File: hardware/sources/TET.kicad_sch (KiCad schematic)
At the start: 43 parts, among them J1 SWD, M1 MountingHole, M2 MountingHole, M3 MountingHole, M4 MountingHole, U1 TCAN330GDCNR, U2 8 MHz, U3 STM32L431RBT6TR, U4 TMP112AIDRLR

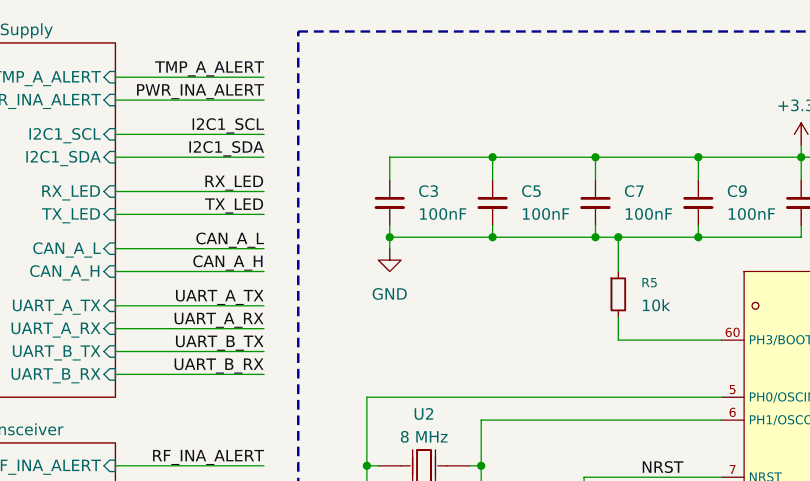
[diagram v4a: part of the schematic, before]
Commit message: hardware(schematic): add bulk capacitor on STM32L4 #5
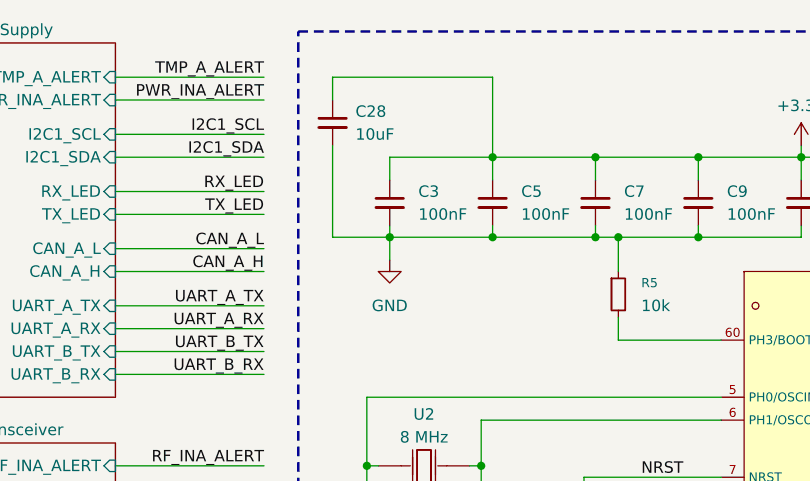
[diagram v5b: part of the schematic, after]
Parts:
- added C28: 10uF, symbol Device:C_Small
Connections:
- net +3.3V: now also C28.1
- net GND: now also C28.2

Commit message: feat(schematic): fix double pull-up resistor for LR_BUSY
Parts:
- removed R2: 10k, Resistor_SMD:R_0603_1608Metric, symbol Device:R_Small
- C28: footprint (none) -> Capacitor_SMD:C_0603_1608Metric
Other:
- moved on the sheet: R1
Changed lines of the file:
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@@
 	)
 	(junction
-		(at 62.23 101.6)
-		(diameter 0)
-		(color 0 0 0 0)
-	)
-	(junction
 		(at 154.94 27.94)
 		(diameter 0)
@@
 	(wire
 		(pts
-			(xy 69.85 101.6) (xy 69.85 102.87)
-		)
-		(stroke
-			(width 0)
-			(type default)
-		)
-	)
-	(wire
-		(pts
 			(xy 201.93 30.48) (xy 209.55 30.48)
 		)
@@
 	(wire
 		(pts
-			(xy 62.23 99.06) (xy 62.23 101.6)
+			(xy 71.12 102.87) (xy 71.12 107.95)
 		)
 		(stroke
@@
 	(wire
 		(pts
-			(xy 62.23 115.57) (xy 62.23 111.76)
+			(xy 71.12 115.57) (xy 71.12 113.03)
 		)
 		(stroke
@@
 	(wire
 		(pts
-			(xy 62.23 106.68) (xy 62.23 101.6)
+			(xy 33.02 40.64) (xy 49.53 40.64)
 		)
 		(stroke
@@
 	(wire
 		(pts
-			(xy 33.02 40.64) (xy 49.53 40.64)
+			(xy 177.8 39.37) (xy 177.8 38.1)
 		)
 		(stroke
@@
 	(wire
 		(pts
-			(xy 177.8 39.37) (xy 177.8 38.1)
+			(xy 124.46 134.62) (xy 124.46 135.89)
 		)
 		(stroke
@@
 	(wire
 		(pts
-			(xy 124.46 134.62) (xy 124.46 135.89)
+			(xy 138.43 38.1) (xy 138.43 27.94)
 		)
 		(stroke
@@
 	(wire
 		(pts
-			(xy 138.43 38.1) (xy 138.43 27.94)
+			(xy 73.66 57.15) (xy 73.66 62.23)
 		)
 		(stroke
@@
 	(wire
 		(pts
-			(xy 73.66 57.15) (xy 73.66 62.23)
+			(xy 148.59 102.87) (xy 166.37 102.87)
 		)
 		(stroke
@@
 	(wire
 		(pts
-			(xy 148.59 102.87) (xy 166.37 102.87)
+			(xy 200.66 140.97) (xy 203.2 140.97)
 		)
 		(stroke
@@
 	(wire
 		(pts
-			(xy 200.66 140.97) (xy 203.2 140.97)
+			(xy 80.01 110.49) (xy 100.33 110.49)
 		)
 		(stroke
@@
 	(wire
 		(pts
-			(xy 62.23 115.57) (xy 100.33 115.57)
+			(xy 71.12 115.57) (xy 100.33 115.57)
 		)
 		(stroke
@@
 	(wire
 		(pts
-			(xy 69.85 110.49) (xy 100.33 110.49)
-		)
-		(stroke
-			(width 0)
-			(type default)
-		)
-	)
-	(wire
-		(pts
 			(xy 148.59 74.93) (xy 161.29 74.93)
 		)
@@
 	(wire
 		(pts
-			(xy 62.23 101.6) (xy 69.85 101.6)
-		)
-		(stroke
-			(width 0)
-			(type default)
-		)
-	)
-	(wire
-		(pts
 			(xy 40.64 186.69) (xy 40.64 193.04)
 		)
@@
 	(wire
 		(pts
-			(xy 69.85 110.49) (xy 69.85 107.95)
-		)
-		(stroke
-			(width 0)
-			(type default)
-		)
-	)
-	(wire
-		(pts
 			(xy 194.31 107.95) (xy 194.31 119.38)
 		)
@@
 	(symbol
 		(lib_id "Device:R_Small")
-		(at 69.85 105.41 0)
-		(unit 1)
-		(body_style 1)
-		(exclude_from_sim no)
-		(in_bom yes)
-		(on_board yes)
-		(in_pos_files yes)
-		(dnp no)
-		(fields_autoplaced yes)
-		(property "Reference" "R2"
-			(at 72.39 104.1399 0)
-			(show_name no)
-			(do_not_autoplace no)
-			(effects
-				(font
-					(size 1.016 1.016)
-				)
-				(justify left)
-			)
-		)
-		(property "Value" "10k"
-			(at 72.39 106.6799 0)
-			(show_name no)
-			(do_not_autoplace no)
-			(effects
-				(font
-					(size 1.27 1.27)
-				)
-				(justify left)
-			)
-		)
-		(property "Footprint" "Resistor_SMD:R_0603_1608Metric"
-			(at 69.85 105.41 0)
-			(hide yes)
-			(show_name no)
-			(do_not_autoplace no)
-			(effects
-				(font
-					(size 1.27 1.27)
-				)
-			)
-		)
-		(property "Datasheet" ""
-			(at 69.85 105.41 0)
-			(hide yes)
-			(show_name no)
-			(do_not_autoplace no)
-			(effects
-				(font
-					(size 1.27 1.27)
-				)
-			)
-		)
-		(property "Description" "Resistor, small symbol"
-			(at 69.85 105.41 0)
-			(hide yes)
-			(show_name no)
-			(do_not_autoplace no)
-			(effects
-				(font
-					(size 1.27 1.27)
-				)
-			)
-		)
-		(pin "2"
-		)
-		(pin "1"
-		)
-		(instances
-			(project "TET"
-				(path "/9ad3bc3a-e567-4764-b6aa-630c8b7f3c7b"
-					(reference "R2")
-					(unit 1)
-				)
-			)
-		)
-	)
-	(symbol
-		(lib_id "Device:R_Small")
 		(at 175.26 100.33 0)
 		(unit 1)
@@
 	(symbol
 		(lib_id "power:+3.3V")
-		(at 62.23 99.06 0)
+		(at 71.12 102.87 0)
 		(unit 1)
 		(body_style 1)
@@
 		(fields_autoplaced yes)
 		(property "Reference" "#PWR03"
-			(at 62.23 102.87 0)
+			(at 71.12 106.68 0)
 			(hide yes)
 			(show_name no)
@@
 		)
 		(property "Value" "+3.3V"
-			(at 62.23 93.98 0)
+			(at 71.12 97.79 0)
 			(show_name no)
 			(do_not_autoplace no)
@@
 		)
 		(property "Footprint" ""
-			(at 62.23 99.06 0)
+			(at 71.12 102.87 0)
 			(hide yes)
 			(show_name no)
@@
 		)
 		(property "Datasheet" ""
-			(at 62.23 99.06 0)
+			(at 71.12 102.87 0)
 			(hide yes)
 			(show_name no)
@@
 		)
 		(property "Description" "Power symbol creates a global label with name \"+3.3V\""
-			(at 62.23 99.06 0)
+			(at 71.12 102.87 0)
 			(hide yes)
 			(show_name no)
@@
 			)
 		)
-		(property "Footprint" ""
+		(property "Footprint" "Capacitor_SMD:C_0603_1608Metric"
 			(at 57.15 24.13 0)
 			(hide yes)
@@
 	(symbol
 		(lib_id "Device:R_Small")
-		(at 62.23 109.22 0)
+		(at 71.12 110.49 0)
 		(unit 1)
 		(body_style 1)
@@
 		(fields_autoplaced yes)
 		(property "Reference" "R1"
-			(at 64.77 107.9499 0)
+			(at 73.66 109.2199 0)
 			(show_name no)
 			(do_not_autoplace no)
@@
 		)
 		(property "Value" "10k"
-			(at 64.77 110.4899 0)
+			(at 73.66 111.7599 0)
 			(show_name no)
 			(do_not_autoplace no)
@@
 		)
 		(property "Footprint" "Resistor_SMD:R_0603_1608Metric"
-			(at 62.23 109.22 0)
+			(at 71.12 110.49 0)
 			(hide yes)
 			(show_name no)
@@
 		)
 		(property "Datasheet" ""
-			(at 62.23 109.22 0)
+			(at 71.12 110.49 0)
 			(hide yes)
 			(show_name no)
@@
 		)
 		(property "Description" "Resistor, small symbol"
-			(at 62.23 109.22 0)
+			(at 71.12 110.49 0)
 			(hide yes)
 			(show_name no)

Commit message: hardware(pcb_design): components Micro-Placement
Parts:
- R3, R4: footprint Resistor_SMD:R_0603_1608Metric -> Resistor_SMD:R_0603_1608Metric_Pad0.98x0.95mm_HandSolder
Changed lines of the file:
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@@
 			)
 		)
-		(property "Footprint" "Resistor_SMD:R_0603_1608Metric"
+		(property "Footprint" "Resistor_SMD:R_0603_1608Metric_Pad0.98x0.95mm_HandSolder"
 			(at 78.74 173.99 0)
 			(hide yes)
@@
 			)
 		)
-		(property "Footprint" "Resistor_SMD:R_0603_1608Metric"
+		(property "Footprint" "Resistor_SMD:R_0603_1608Metric_Pad0.98x0.95mm_HandSolder"
 			(at 78.74 165.1 0)
 			(hide yes)
